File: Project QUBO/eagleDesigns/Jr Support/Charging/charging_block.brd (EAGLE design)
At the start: 85.1 x 77.1 mm, 123 parts

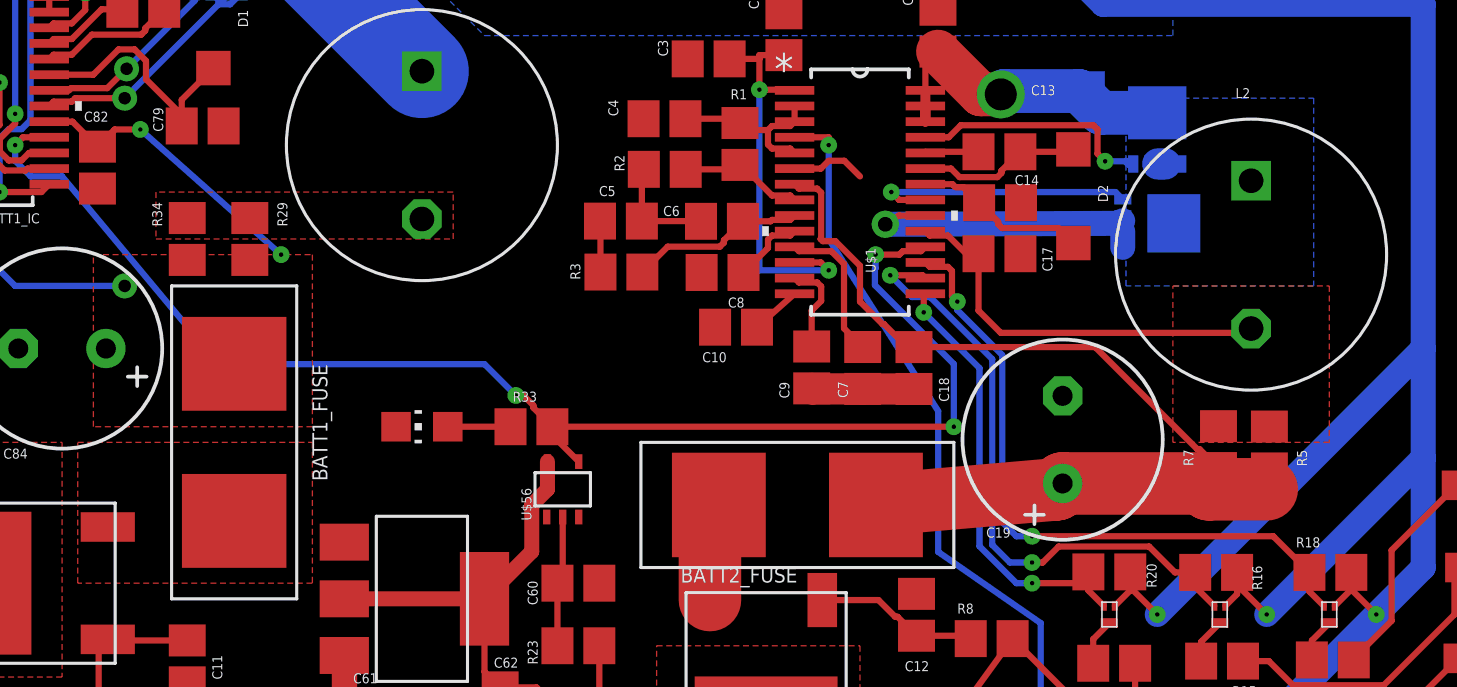
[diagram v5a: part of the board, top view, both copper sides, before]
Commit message: 
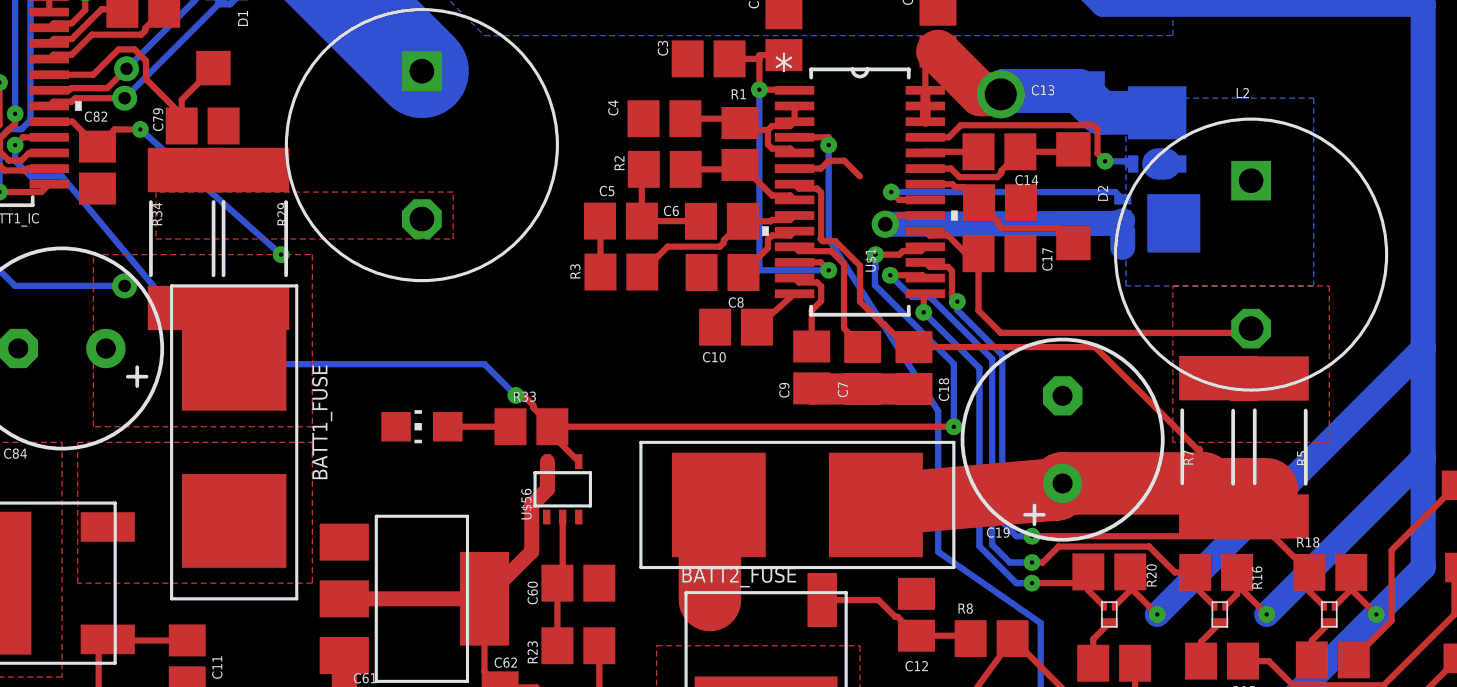
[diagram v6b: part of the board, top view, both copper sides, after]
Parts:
- R29, R34, R5, R7: device resistor:R0805 -> resistor:R2512
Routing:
- net BATT_2: track 41.8 -> 44.6 mm
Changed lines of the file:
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@@
 <?xml version="1.0" encoding="utf-8"?>
 <!DOCTYPE eagle SYSTEM "eagle.dtd">
-<eagle version="8.1.0">
+<eagle version="8.2.0">
 <drawing>
 <settings>
@@
 <layer number="27" name="tValues" color="7" fill="1" visible="yes" active="yes"/>
 <layer number="28" name="bValues" color="7" fill="1" visible="yes" active="yes"/>
-<layer number="29" name="tStop" color="7" fill="3" visible="yes" active="yes"/>
-<layer number="30" name="bStop" color="7" fill="6" visible="yes" active="yes"/>
-<layer number="31" name="tCream" color="7" fill="4" visible="yes" active="yes"/>
-<layer number="32" name="bCream" color="7" fill="5" visible="yes" active="yes"/>
+<layer number="29" name="tStop" color="7" fill="3" visible="no" active="yes"/>
+<layer number="30" name="bStop" color="7" fill="6" visible="no" active="yes"/>
+<layer number="31" name="tCream" color="7" fill="4" visible="no" active="yes"/>
+<layer number="32" name="bCream" color="7" fill="5" visible="no" active="yes"/>
 <layer number="33" name="tFinish" color="6" fill="3" visible="no" active="yes"/>
 <layer number="34" name="bFinish" color="6" fill="6" visible="no" active="yes"/>
@@
 <layer number="46" name="Milling" color="3" fill="1" visible="no" active="yes"/>
 <layer number="47" name="Measures" color="7" fill="1" visible="no" active="yes"/>
-<layer number="48" name="Document" color="7" fill="1" visible="yes" active="yes"/>
-<layer number="49" name="Reference" color="7" fill="1" visible="yes" active="yes"/>
+<layer number="48" name="Document" color="7" fill="1" visible="no" active="yes"/>
+<layer number="49" name="Reference" color="7" fill="1" visible="no" active="yes"/>
 <layer number="50" name="dxf" color="7" fill="1" visible="no" active="no"/>
 <layer number="51" name="tDocu" color="7" fill="1" visible="yes" active="yes"/>
-<layer number="52" name="bDocu" color="7" fill="1" visible="no" active="yes"/>
+<layer number="52" name="bDocu" color="7" fill="1" visible="yes" active="yes"/>
 <layer number="53" name="tGND_GNDA" color="7" fill="9" visible="no" active="no"/>
 <layer number="54" name="bGND_GNDA" color="1" fill="9" visible="no" active="no"/>
@@
 <attribute name="VALUE" x="74.803" y="39.624" size="0.4064" layer="27" ratio="7"/>
 </element>
-<element name="R29" library="resistor" package="R0805" value="100m" x="49.53" y="59.055" smashed="yes" rot="R90">
+<element name="R29" library="resistor" package="R2512" value="100m" x="49.53" y="59.055" smashed="yes" rot="R90">
 <attribute name="NAME" x="51.054" y="59.563" size="0.4064" layer="25" ratio="7" rot="R90"/>
 <attribute name="VALUE" x="50.292" y="60.706" size="0.4064" layer="27" ratio="7" rot="R180"/>
@@
 <attribute name="VALUE" x="26.141103125" y="66.970928125" size="0.4064" layer="27" ratio="7"/>
 </element>
-<element name="R34" library="resistor" package="R0805" value="100m" x="46.99" y="59.055" smashed="yes" rot="R90">
+<element name="R34" library="resistor" package="R2512" value="100m" x="46.99" y="59.055" smashed="yes" rot="R90">
 <attribute name="NAME" x="45.974" y="59.563" size="0.4064" layer="25" ratio="7" rot="R90"/>
 <attribute name="VALUE" x="47.752" y="60.706" size="0.4064" layer="27" ratio="7" rot="R180"/>
@@
 <attribute name="VALUE" x="43.942" y="39.116" size="0.4064" layer="27" ratio="7" rot="R180"/>
 </element>
-<element name="R5" library="resistor" package="R0805" value="100m" x="90.91331875" y="50.59105625" smashed="yes" rot="R90">
+<element name="R5" library="resistor" package="R2512" value="100m" x="90.91331875" y="50.59105625" smashed="yes" rot="R90">
 <attribute name="NAME" x="92.43731875" y="49.82905625" size="0.4064" layer="25" ratio="7" rot="R90"/>
 <attribute name="VALUE" x="90.46905625" y="48.40568125" size="0.4064" layer="27" ratio="7"/>
@@
 <attribute name="VALUE" x="39.497" y="39.116" size="0.4064" layer="27" ratio="7" rot="R180"/>
 </element>
-<element name="R7" library="resistor" package="R0805" value="100m" x="88.846809375" y="50.606625" smashed="yes" rot="R90">
+<element name="R7" library="resistor" package="R2512" value="100m" x="88.846809375" y="50.606625" smashed="yes" rot="R90">
 <attribute name="NAME" x="87.830809375" y="49.844625" size="0.4064" layer="25" ratio="7" rot="R90"/>
 <attribute name="VALUE" x="87.944625" y="48.567190625" size="0.4064" layer="27" ratio="7"/>
@@
 <vertex x="45.72" y="60.96"/>
 </polygon>
-<wire x1="49.53" y1="59.905" x2="50.8" y2="58.42" width="0" layer="19" extent="1-1"/>
+<wire x1="46.99" y1="61.855" x2="45.085" y2="63.5" width="0" layer="19" extent="1-16"/>
 </signal>
 <signal name="N$84">
@@
 <wire x1="89.995" y1="55.245" x2="90.17" y2="55.42" width="0.254" layer="1"/>
 <wire x1="80.01" y1="55.245" x2="89.995" y2="55.245" width="0.254" layer="1"/>
+<wire x1="88.846809375" y1="53.406625" x2="90.91331875" y2="53.39105625" width="0" layer="19" extent="1-1"/>
+<wire x1="89.995" y1="55.245" x2="90.91331875" y2="53.39105625" width="0" layer="19" extent="1-1"/>
 </signal>
 <signal name="THM_2">
@@
 <wire x1="82.2824" y1="48.895" x2="82.5196375" y2="49.1322375" width="2.54" layer="1"/>
 <wire x1="88.222421875" y1="49.1322375" x2="82.5196375" y2="49.1322375" width="2.54" layer="1"/>
-<wire x1="90.91331875" y1="49.74105625" x2="90.91331875" y2="49.00331875" width="0.254" layer="1"/>
+<wire x1="90.91331875" y1="47.79105625" x2="90.91331875" y2="49.00331875" width="0.254" layer="1"/>
 <wire x1="90.91331875" y1="49.00331875" x2="90.805" y2="48.895" width="0.254" layer="1"/>
 <wire x1="90.805" y1="48.895" x2="88.459659375" y2="48.895" width="2.54" layer="1"/>
 <wire x1="88.459659375" y1="48.895" x2="88.222421875" y2="49.1322375" width="2.54" layer="1"/>
-<wire x1="88.846809375" y1="49.756625" x2="88.222421875" y2="49.1322375" width="0.254" layer="1"/>
+<wire x1="88.846809375" y1="47.806625" x2="88.222421875" y2="49.1322375" width="0.254" layer="1"/>
 <wire x1="87.981078125" y1="50.527225" x2="88.076209375" y2="50.527225" width="0.254" layer="1"/>
-<wire x1="88.076209375" y1="50.527225" x2="88.846809375" y2="49.756625" width="0.254" layer="1"/>
+<wire x1="88.076209375" y1="50.527225" x2="88.846809375" y2="47.806625" width="0.254" layer="1"/>
 <wire x1="83.8415625" y1="54.666740625" x2="76.486875" y2="54.666740625" width="0.254" layer="1"/>
 <wire x1="83.8415625" y1="54.666740625" x2="87.981078125" y2="50.527225" width="0.254" layer="1"/>
